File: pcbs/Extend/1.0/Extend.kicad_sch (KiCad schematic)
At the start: 24 parts, among them J1 Conn_01x06_Pin, J10 Conn_01x02_Male, J13 Conn_01x04_Pin, J2 Conn_01x05_Pin, J3 Conn_01x04_Pin, J4 Conn_01x02_Male, J5 Conn_01x02_Male, J6 Conn_01x02_Male, J7 Conn_01x02_Pin, J8 Conn_01x05_Pin, J9 Conn_01x02_Pin, U1 MCP23017_SS

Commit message: Updates
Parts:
- renumbered C3 to C2, C4 to C3, H3 to H2, H2 to H3, J5 to J1, J6 to J10, J9 to J11, J8 to J2, J1 to J4, J4 to J5, J10 to J6, J13 to J7, J2 to J8, J7 to J9, R3 to R1, R4 to R2, R2 to R3, R1 to R4
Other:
- moved on the sheet: C1, C2, C3, D1, J10, J11, J2, J4, J5, J6, J9, R1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

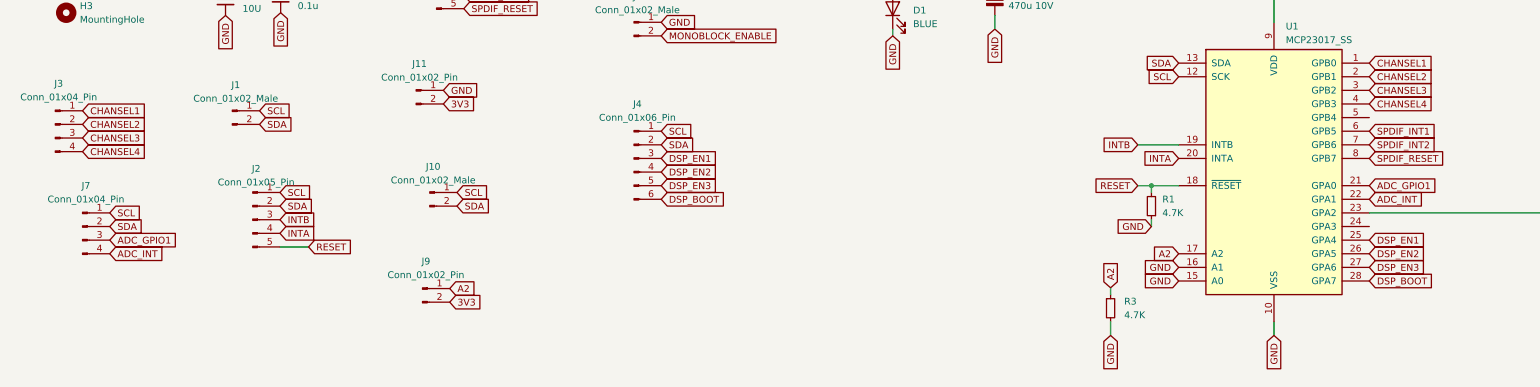
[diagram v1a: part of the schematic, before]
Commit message: Updated screenshots
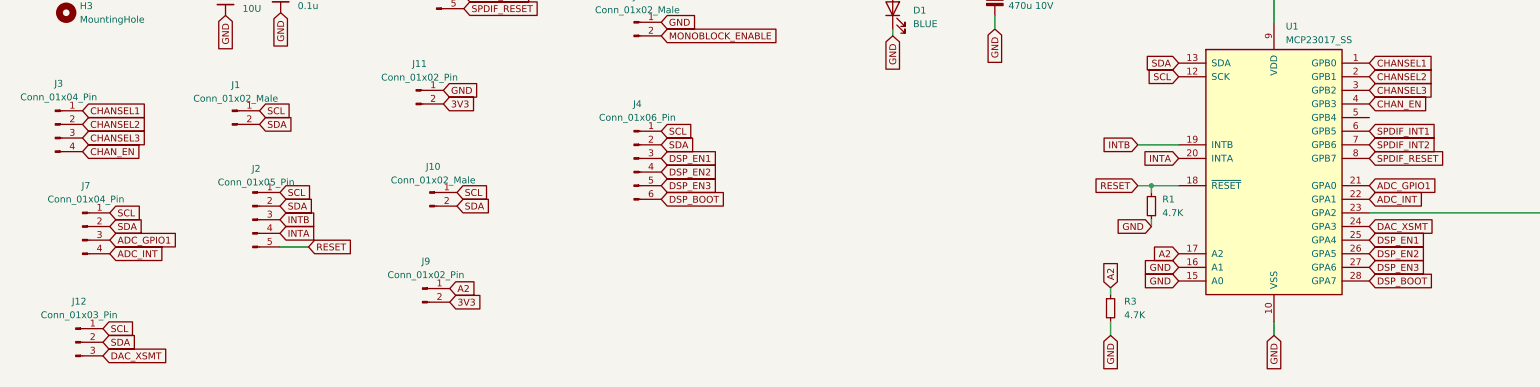
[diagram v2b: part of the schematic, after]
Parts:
- added J12: Conn_01x03_Pin, Connector_JST:JST_PH_B3B-PH-K_1x03_P2.00mm_Vertical, symbol Connector:Conn_01x03_Pin
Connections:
- net SCL: now also J12.1 (Pin_1)
- net SDA: now also J12.2 (Pin_2)
- net DAC_XSMT: now reaches U1.24 (GPA3)
- net DAC_XSMT: now also J12.3 (Pin_3)
- net CHANSEL4 renamed CHAN_EN
